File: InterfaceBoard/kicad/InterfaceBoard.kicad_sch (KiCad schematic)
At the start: 48 parts, among them J1 MIDI IN, J10 JST Portamento Pot, J3 JST MIDI IN, J4 AudioJack2, J5 JST MIDI THRU, J6 JST GATE IN, J7 JST GATE CTRL, J8 JST Pitch Adj., J9 JST PWR, Q1 2N7000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

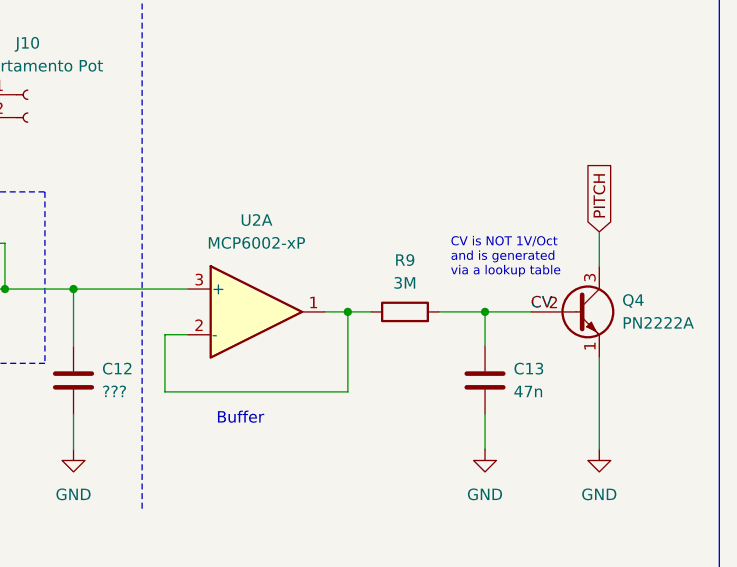
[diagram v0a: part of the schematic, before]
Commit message: Interface board: Initial README commit
Signed-off-by: CTXz <ctx.xda@gmail.com>
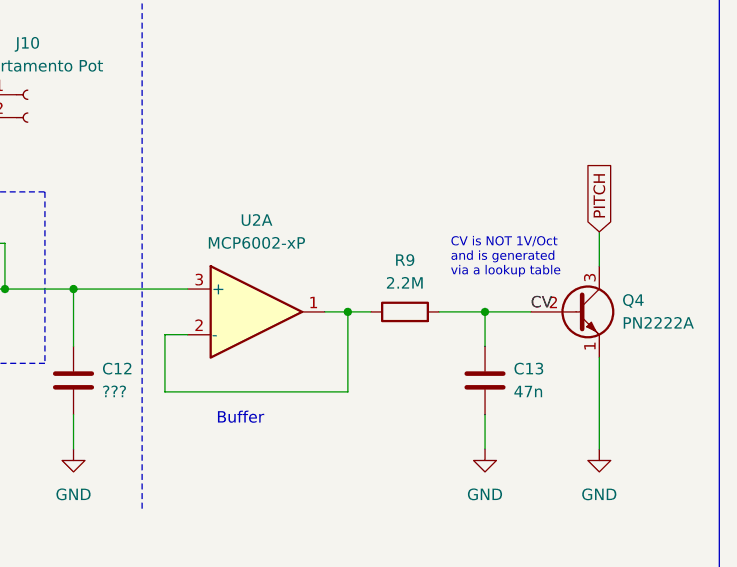
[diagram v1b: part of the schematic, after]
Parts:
- R9: value 3M -> 2.2M
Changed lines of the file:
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@@
       (effects (font (size 1.27 1.27)))
     )
-    (property "Value" "3M" (at 372.745 201.295 90)
+    (property "Value" "2.2M" (at 372.745 201.295 90)
       (effects (font (size 1.27 1.27)))
     )

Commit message: Minor updates
Signed-off-by: CTXz <ctx.xda@gmail.com>
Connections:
- net GATE JACK renamed GATE JACK + HOLD
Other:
- note added: "OR'd Gate Control This eliminates the need to incorporate an additional switch, although it does allow both inputs to potentially activate the GATE simultaneously, regardless of whether MIDI is selected as a CV source or not."
- note removed: "ANDed Gate Control This eliminates the need to incorporate an additional switch, although it does allow both inputs to potentially activate the GATE simultaneously, regardless of whether MIDI is selected as a CV source or not."
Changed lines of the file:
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@@
     (effects (font (size 1.27 1.27)) (justify left bottom))
   )
-  (text "ANDed Gate Control\n\nThis eliminates the need to\nincorporate an additional switch,\nalthough it does allow both inputs\nto potentially activate the GATE\nsimultaneously, regardless of whether\nMIDI is selected as a CV source or not."
+  (text "OR'd Gate Control\n\nThis eliminates the need to\nincorporate an additional switch,\nalthough it does allow both inputs\nto potentially activate the GATE\nsimultaneously, regardless of whether\nMIDI is selected as a CV source or not."
     (at 344.17 63.5 0)
     (effects (font (size 1.27 1.27)) (justify left bottom))
@@
     )
   )
-  (global_label "GATE JACK" (shape input) (at 301.625 70.485 180) (fields_autoplaced)
+  (global_label "GATE JACK + HOLD" (shape input) (at 301.625 70.485 180) (fields_autoplaced)
     (effects (font (size 1.27 1.27)) (justify right))
-    (property "Intersheetrefs" "${INTERSHEET_REFS}" (at 288.6008 70.485 0)
+    (property "Intersheetrefs" "${INTERSHEET_REFS}" (at 280.1341 70.485 0)
       (effects (font (size 1.27 1.27)) (justify right) hide)
     )
   )
-  (global_label "GATE JACK" (shape output) (at 104.14 225.425 0) (fields_autoplaced)
+  (global_label "GATE JACK + HOLD" (shape output) (at 104.14 225.425 0) (fields_autoplaced)
     (effects (font (size 1.27 1.27)) (justify left))
-    (property "Intersheetrefs" "${INTERSHEET_REFS}" (at 117.1642 225.425 0)
+    (property "Intersheetrefs" "${INTERSHEET_REFS}" (at 125.6309 225.425 0)
       (effects (font (size 1.27 1.27)) (justify left) hide)
     )
